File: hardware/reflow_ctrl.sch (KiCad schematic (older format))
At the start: 18 parts, among them IC1 MAX6675, U2 MOC3063, U3 BTA41/600B, X2 Mains, X3 Load, X4 Thermocouple

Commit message: ERC clean
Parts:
- gave numbers to parts that had none: 3
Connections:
- wire segments 49 -> 52
- no-connect marks 1 -> 5
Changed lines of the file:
@@
 L_load
 $Comp
-L GND #PWR01
+L GND #PWR7
 U 1 1 56A9FAD0
 P 6250 2150
-F 0 "#PWR01" H 6250 1900 50  0001 C CNN
+F 0 "#PWR7" H 6250 1900 50  0001 C CNN
 F 1 "GND" H 6250 2000 50  0000 C CNN
 F 2 "" H 6250 2150 60  0000 C CNN
@@
 $EndComp
 $Comp
-L GND #PWR02
+L GND #PWR9
 U 1 1 56AA0C93
 P 8200 5000
-F 0 "#PWR02" H 8200 4750 50  0001 C CNN
+F 0 "#PWR9" H 8200 4750 50  0001 C CNN
 F 1 "GND" H 8200 4850 50  0000 C CNN
 F 2 "" H 8200 5000 60  0000 C CNN
@@
 TODO\n* Complete supplier links\n* Add 3 Switches and approx. 3 LEDs\n* Add netclasses
 $Comp
-L CONN_02X05 X?
+L CONN_02X05 X1
 U 1 1 56C0B2E0
 P 3150 3400
-F 0 "X?" H 3150 3700 50  0000 C CNN
+F 0 "X1" H 3150 3700 50  0000 C CNN
 F 1 "Master" H 3150 3100 50  0000 C CNN
 F 2 "" H 3150 2200 60  0000 C CNN
@@
 $EndComp
 $Comp
-L +3.3V #PWR?
+L +3.3V #PWR8
 U 1 1 56C0C614
 P 8200 4600
-F 0 "#PWR?" H 8200 4450 50  0001 C CNN
+F 0 "#PWR8" H 8200 4450 50  0001 C CNN
 F 1 "+3.3V" H 8200 4740 50  0000 C CNN
 F 2 "" H 8200 4600 60  0000 C CNN
@@
 $EndComp
 $Comp
-L +3.3V #PWR?
+L +3.3V #PWR3
 U 1 1 56C0C64E
-P 2850 3150
-F 0 "#PWR?" H 2850 3000 50  0001 C CNN
-F 1 "+3.3V" H 2850 3290 50  0000 C CNN
-F 2 "" H 2850 3150 60  0000 C CNN
-F 3 "" H 2850 3150 60  0000 C CNN
-	1    2850 3150
-	1    0    0    -1
-$EndComp
-Wire Wire Line
-	2850 3150 2850 3200
+P 2850 2950
+F 0 "#PWR3" H 2850 2800 50  0001 C CNN
+F 1 "+3.3V" H 2850 3090 50  0000 C CNN
+F 2 "" H 2850 2950 60  0000 C CNN
+F 3 "" H 2850 2950 60  0000 C CNN
+	1    2850 2950
+	1    0    0    -1
+$EndComp
+Wire Wire Line
+	2850 2950 2850 3200
 Wire Wire Line
 	2850 3200 2900 3200
 $Comp
-L GND #PWR?
+L GND #PWR4
 U 1 1 56C0CE3A
 P 3450 3650
-F 0 "#PWR?" H 3450 3400 50  0001 C CNN
+F 0 "#PWR4" H 3450 3400 50  0001 C CNN
 F 1 "GND" H 3450 3500 50  0000 C CNN
 F 2 "" H 3450 3650 60  0000 C CNN
@@
 	3450 3600 3450 3650
 $Comp
-L C C?
+L C C1
 U 1 1 56C0D9F5
 P 1800 3350
-F 0 "C?" H 1800 3450 50  0000 L CNN
+F 0 "C1" H 1800 3450 50  0000 L CNN
 F 1 "100n" H 1800 3250 50  0000 L CNN
 F 2 "Capacitors_SMD:C_0603" H 1838 3200 30  0001 C CNN
@@
 $EndComp
 $Comp
-L C C?
+L C C2
 U 1 1 56C209CA
 P 2100 3350
-F 0 "C?" H 2100 3450 50  0000 L CNN
+F 0 "C2" H 2100 3450 50  0000 L CNN
 F 1 "100n" H 2100 3250 50  0000 L CNN
 F 2 "Capacitors_SMD:C_0603" H 2138 3200 30  0001 C CNN
@@
 $EndComp
 $Comp
-L GND #PWR?
+L GND #PWR2
 U 1 1 56C20A24
 P 1950 3600
-F 0 "#PWR?" H 1950 3350 50  0001 C CNN
+F 0 "#PWR2" H 1950 3350 50  0001 C CNN
 F 1 "GND" H 1950 3450 50  0000 C CNN
 F 2 "" H 1950 3600 60  0000 C CNN
@@
 Connection ~ 1950 3550
 $Comp
-L +3.3V #PWR?
+L +3.3V #PWR1
 U 1 1 56C20AF7
 P 1950 3100
-F 0 "#PWR?" H 1950 2950 50  0001 C CNN
+F 0 "#PWR1" H 1950 2950 50  0001 C CNN
 F 1 "+3.3V" H 1950 3240 50  0000 C CNN
 F 2 "" H 1950 3100 60  0000 C CNN
@@
 	1950 3100 1950 3150
 Connection ~ 1950 3150
+NoConn ~ 3400 3200
+NoConn ~ 3400 3300
+NoConn ~ 2900 3300
+NoConn ~ 3400 3400
+$Comp
+L PWR_FLAG #FLG1
+U 1 1 56C22014
+P 5900 7000
+F 0 "#FLG1" H 5900 7095 50  0001 C CNN
+F 1 "PWR_FLAG" V 5900 7350 50  0000 C CNN
+F 2 "" H 5900 7000 60  0000 C CNN
+F 3 "" H 5900 7000 60  0000 C CNN
+	1    5900 7000
+	0    1    1    0
+$EndComp
+$Comp
+L PWR_FLAG #FLG2
+U 1 1 56C22108
+P 5900 7200
+F 0 "#FLG2" H 5900 7295 50  0001 C CNN
+F 1 "PWR_FLAG" V 5900 7550 50  0000 C CNN
+F 2 "" H 5900 7200 60  0000 C CNN
+F 3 "" H 5900 7200 60  0000 C CNN
+	1    5900 7200
+	0    1    1    0
+$EndComp
+$Comp
+L GND #PWR6
+U 1 1 56C22149
+P 5850 7250
+F 0 "#PWR6" H 5850 7000 50  0001 C CNN
+F 1 "GND" H 5850 7100 50  0000 C CNN
+F 2 "" H 5850 7250 60  0000 C CNN
+F 3 "" H 5850 7250 60  0000 C CNN
+	1    5850 7250
+	1    0    0    -1
+$EndComp
+Wire Wire Line
+	5850 7250 5850 7200
+Wire Wire Line
+	5850 7200 5900 7200
+$Comp
+L +3.3V #PWR5
+U 1 1 56C22402
+P 5850 7000
+F 0 "#PWR5" H 5850 6850 50  0001 C CNN
+F 1 "+3.3V" H 5850 7140 50  0000 C CNN
+F 2 "" H 5850 7000 60  0000 C CNN
+F 3 "" H 5850 7000 60  0000 C CNN
+	1    5850 7000
+	0    -1   -1   0
+$EndComp
+Wire Wire Line
+	5850 7000 5900 7000
 $EndSCHEMATC

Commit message: Update board
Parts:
- X1: footprint (none) -> uMIDI:Con-boxed_header-THT
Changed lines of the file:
@@
 F 0 "X1" H 3150 3700 50  0000 C CNN
 F 1 "Master" H 3150 3100 50  0000 C CNN
-F 2 "" H 3150 2200 60  0000 C CNN
+F 2 "uMIDI:Con-boxed_header-THT" H 3150 2200 60  0001 C CNN
 F 3 "" H 3150 2200 60  0000 C CNN
 	1    3150 3400

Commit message: Prepare net classes
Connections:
- net labels added: L_main_fused, MOC_A1, MOC_A2, Snub
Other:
- moved on the sheet: C12, R6
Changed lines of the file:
@@
 L R R6
 U 1 1 56A9031F
-P 8550 1700
-F 0 "R6" V 8630 1700 50  0000 C CNN
-F 1 "39" V 8550 1700 50  0000 C CNN
-F 2 "Resistors_SMD:R_1206" V 8480 1700 30  0001 C CNN
-F 3 "" H 8550 1700 30  0000 C CNN
-	1    8550 1700
+P 8550 1650
+F 0 "R6" V 8630 1650 50  0000 C CNN
+F 1 "39" V 8550 1650 50  0000 C CNN
+F 2 "Resistors_SMD:R_1206" V 8480 1650 30  0001 C CNN
+F 3 "" H 8550 1650 30  0000 C CNN
+	1    8550 1650
 	1    0    0    -1
 $EndComp
@@
 L C C12
 U 1 1 56A90389
-P 8550 2200
-F 0 "C12" H 8650 2350 50  0000 L CNN
-F 1 "10n" H 8650 2250 50  0000 L CNN
-F 2 "Capacitors_SMD:C_1206" H 8588 2050 30  0001 C CNN
-F 3 "" H 8550 2200 60  0000 C CNN
-F 4 "630V" H 8650 2050 60  0000 L CNN "Voltage"
-F 5 "X7R" H 8650 2150 60  0000 L CNN "Dielectric"
-	1    8550 2200
+P 8550 2300
+F 0 "C12" H 8650 2450 50  0000 L CNN
+F 1 "10n" H 8650 2350 50  0000 L CNN
+F 2 "Capacitors_SMD:C_1206" H 8588 2150 30  0001 C CNN
+F 3 "" H 8550 2300 60  0000 C CNN
+F 4 "630V" H 8650 2150 60  0000 L CNN "Voltage"
+F 5 "X7R" H 8650 2250 60  0000 L CNN "Dielectric"
+	1    8550 2300
 	1    0    0    -1
 $EndComp
@@
 L_load
 $Comp
-L GND #PWR7
+L GND #PWR01
 U 1 1 56A9FAD0
 P 6250 2150
-F 0 "#PWR7" H 6250 1900 50  0001 C CNN
+F 0 "#PWR01" H 6250 1900 50  0001 C CNN
 F 1 "GND" H 6250 2000 50  0000 C CNN
 F 2 "" H 6250 2150 60  0000 C CNN
@@
 $EndComp
 $Comp
-L GND #PWR9
+L GND #PWR02
 U 1 1 56AA0C93
 P 8200 5000
-F 0 "#PWR9" H 8200 4750 50  0001 C CNN
+F 0 "#PWR02" H 8200 4750 50  0001 C CNN
 F 1 "GND" H 8200 4850 50  0000 C CNN
 F 2 "" H 8200 5000 60  0000 C CNN
@@
 	7000 2650 10200 2650
 Wire Wire Line
-	8550 2350 8550 2650
-Wire Wire Line
-	8550 2050 8550 1850
+	8550 2450 8550 2650
+Wire Wire Line
+	8550 2150 8550 1800
 Wire Wire Line
 	7000 1450 7000 1350
@@
 	7000 1350 9350 1350
 Wire Wire Line
-	8550 1550 8550 1350
+	8550 1500 8550 1350
 Connection ~ 8550 1350
 Connection ~ 7000 2100
@@
 $EndComp
 $Comp
-L +3.3V #PWR8
+L +3.3V #PWR03
 U 1 1 56C0C614
 P 8200 4600
-F 0 "#PWR8" H 8200 4450 50  0001 C CNN
+F 0 "#PWR03" H 8200 4450 50  0001 C CNN
 F 1 "+3.3V" H 8200 4740 50  0000 C CNN
 F 2 "" H 8200 4600 60  0000 C CNN
@@
 $EndComp
 $Comp
-L +3.3V #PWR3
+L +3.3V #PWR04
 U 1 1 56C0C64E
 P 2850 2950
-F 0 "#PWR3" H 2850 2800 50  0001 C CNN
+F 0 "#PWR04" H 2850 2800 50  0001 C CNN
 F 1 "+3.3V" H 2850 3090 50  0000 C CNN
 F 2 "" H 2850 2950 60  0000 C CNN
@@
 	2850 3200 2900 3200
 $Comp
-L GND #PWR4
+L GND #PWR05
 U 1 1 56C0CE3A
 P 3450 3650
-F 0 "#PWR4" H 3450 3400 50  0001 C CNN
+F 0 "#PWR05" H 3450 3400 50  0001 C CNN
 F 1 "GND" H 3450 3500 50  0000 C CNN
 F 2 "" H 3450 3650 60  0000 C CNN
@@
 $EndComp
 $Comp
-L GND #PWR2
+L GND #PWR06
 U 1 1 56C20A24
 P 1950 3600
-F 0 "#PWR2" H 1950 3350 50  0001 C CNN
+F 0 "#PWR06" H 1950 3350 50  0001 C CNN
 F 1 "GND" H 1950 3450 50  0000 C CNN
 F 2 "" H 1950 3600 60  0000 C CNN
@@
 Connection ~ 1950 3550
 $Comp
-L +3.3V #PWR1
+L +3.3V #PWR07
 U 1 1 56C20AF7
 P 1950 3100
-F 0 "#PWR1" H 1950 2950 50  0001 C CNN
+F 0 "#PWR07" H 1950 2950 50  0001 C CNN
 F 1 "+3.3V" H 1950 3240 50  0000 C CNN
 F 2 "" H 1950 3100 60  0000 C CNN
@@
 NoConn ~ 3400 3400
 $Comp
-L PWR_FLAG #FLG1
+L PWR_FLAG #FLG08
 U 1 1 56C22014
 P 5900 7000
-F 0 "#FLG1" H 5900 7095 50  0001 C CNN
+F 0 "#FLG08" H 5900 7095 50  0001 C CNN
 F 1 "PWR_FLAG" V 5900 7350 50  0000 C CNN
 F 2 "" H 5900 7000 60  0000 C CNN
@@
 $EndComp
 $Comp
-L PWR_FLAG #FLG2
+L PWR_FLAG #FLG09
 U 1 1 56C22108
 P 5900 7200
-F 0 "#FLG2" H 5900 7295 50  0001 C CNN
+F 0 "#FLG09" H 5900 7295 50  0001 C CNN
 F 1 "PWR_FLAG" V 5900 7550 50  0000 C CNN
 F 2 "" H 5900 7200 60  0000 C CNN
@@
 $EndComp
 $Comp
-L GND #PWR6
+L GND #PWR010
 U 1 1 56C22149
 P 5850 7250
-F 0 "#PWR6" H 5850 7000 50  0001 C CNN
+F 0 "#PWR010" H 5850 7000 50  0001 C CNN
 F 1 "GND" H 5850 7100 50  0000 C CNN
 F 2 "" H 5850 7250 60  0000 C CNN
@@
 	5850 7200 5900 7200
 $Comp
-L +3.3V #PWR5
+L +3.3V #PWR011
 U 1 1 56C22402
 P 5850 7000
-F 0 "#PWR5" H 5850 6850 50  0001 C CNN
+F 0 "#PWR011" H 5850 6850 50  0001 C CNN
 F 1 "+3.3V" H 5850 7140 50  0000 C CNN
 F 2 "" H 5850 7000 60  0000 C CNN
@@
 Wire Wire Line
 	5850 7000 5900 7000
+Text Label 6950 1900 0    60   ~ 0
+MOC_A1
+Text Label 6950 2100 0    60   ~ 0
+MOC_A2
+Text Label 8550 2100 1    60   ~ 0
+Snub
+Text Label 8350 1350 0    60   ~ 0
+L_main_fused
 $EndSCHEMATC

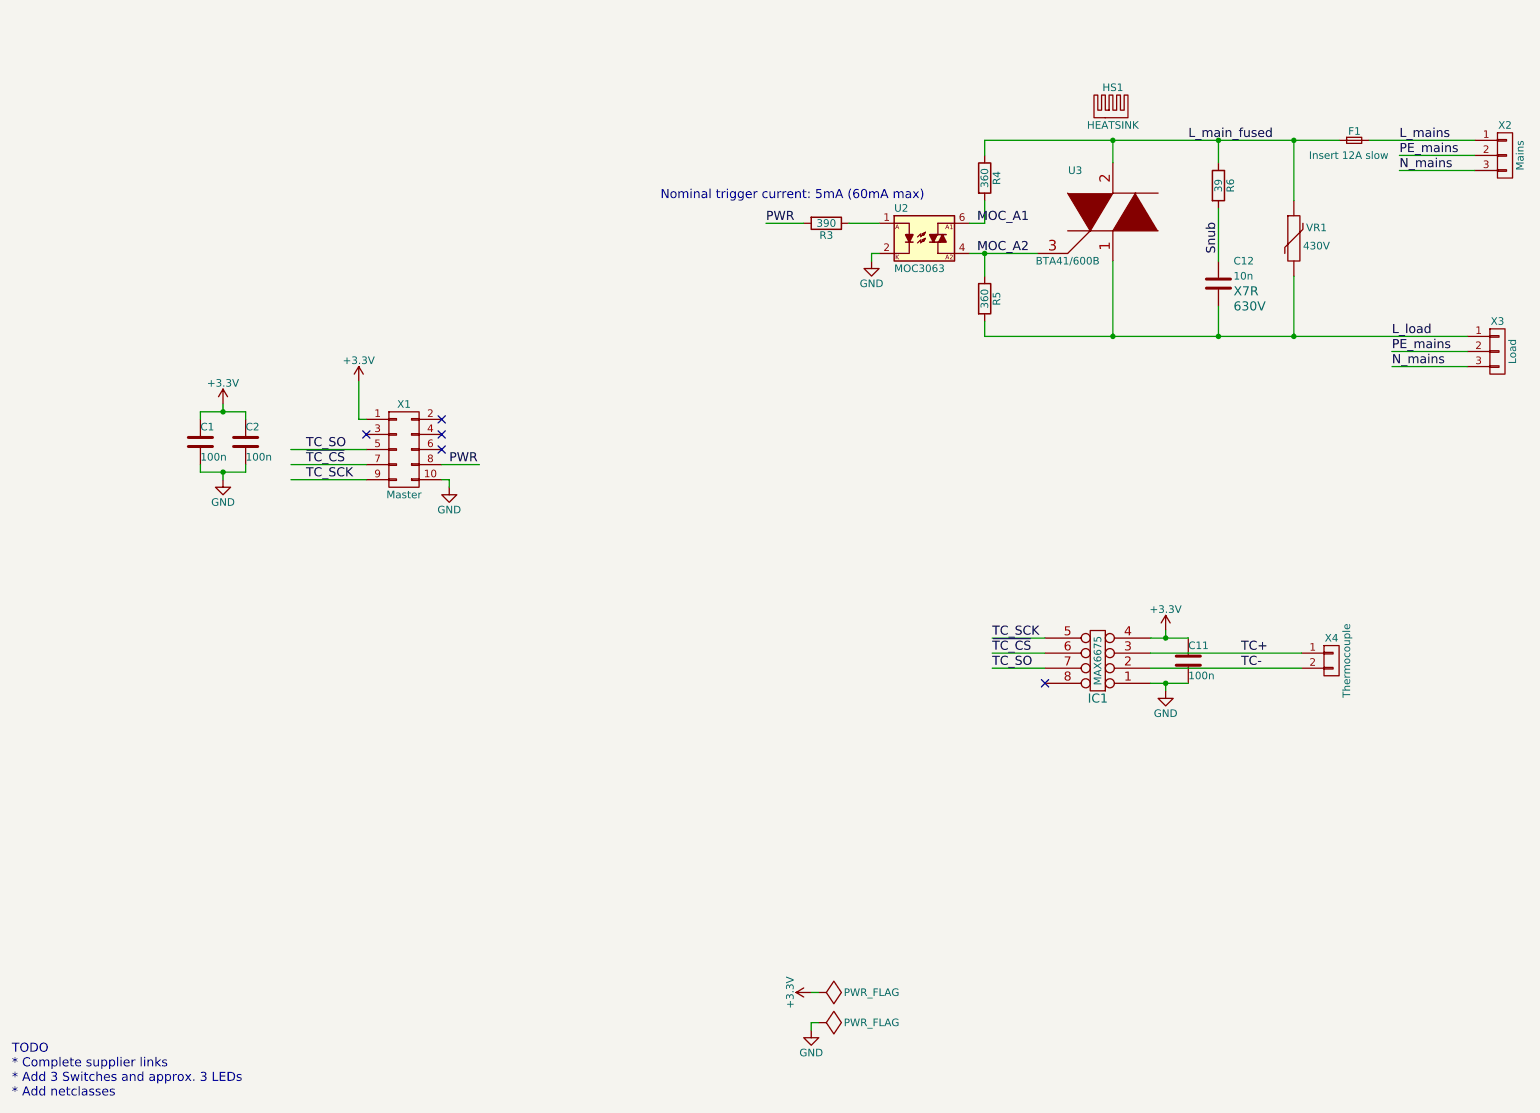
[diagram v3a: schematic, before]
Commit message: Shrink schematic page size
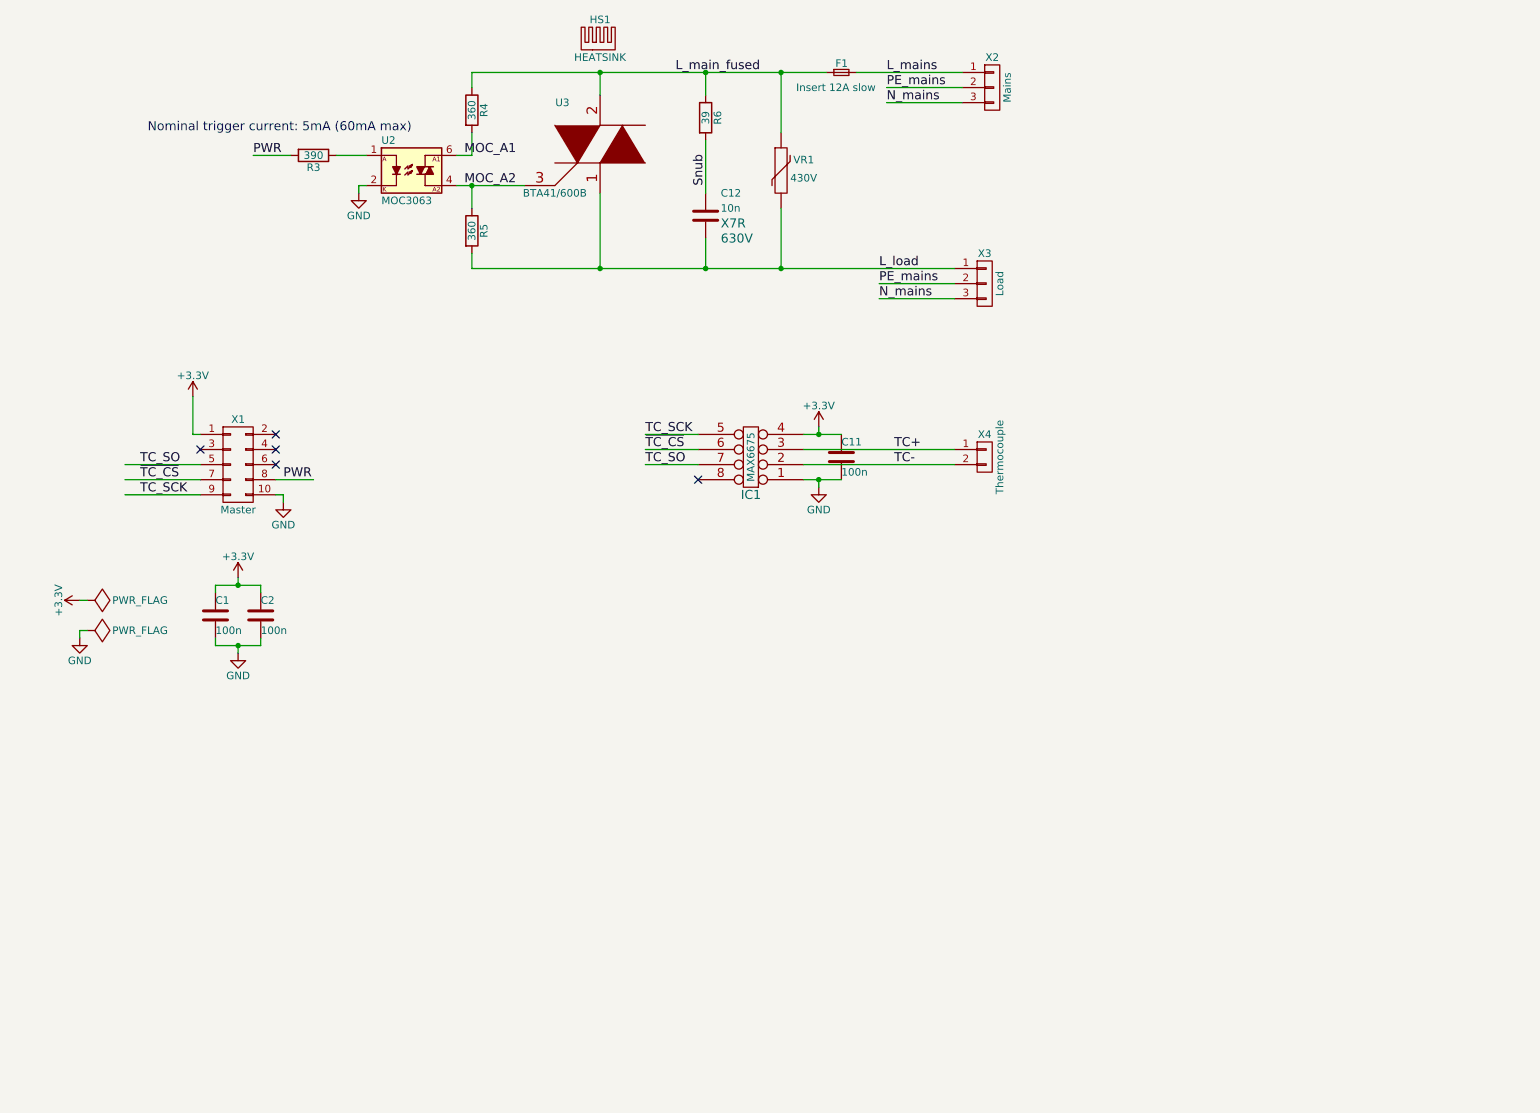
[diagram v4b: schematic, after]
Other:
- note removed: "TODO\n* Complete supplier links\n* Add 3 Switches and approx. 3 LEDs\n* Add netclasses"
- moved on the sheet: C1, C11, C12, C2, F1, HS1, IC1, R3, R4, R5, R6, U2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

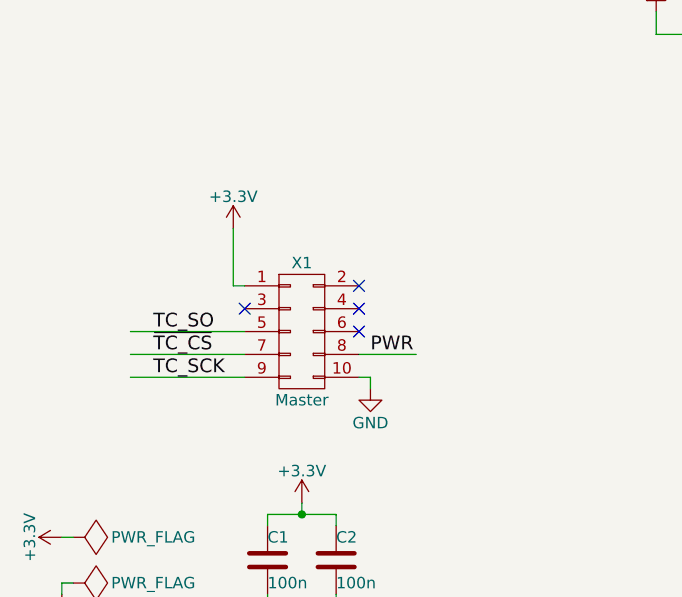
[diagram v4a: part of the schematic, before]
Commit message: Disentangle connector pinout; Start placement
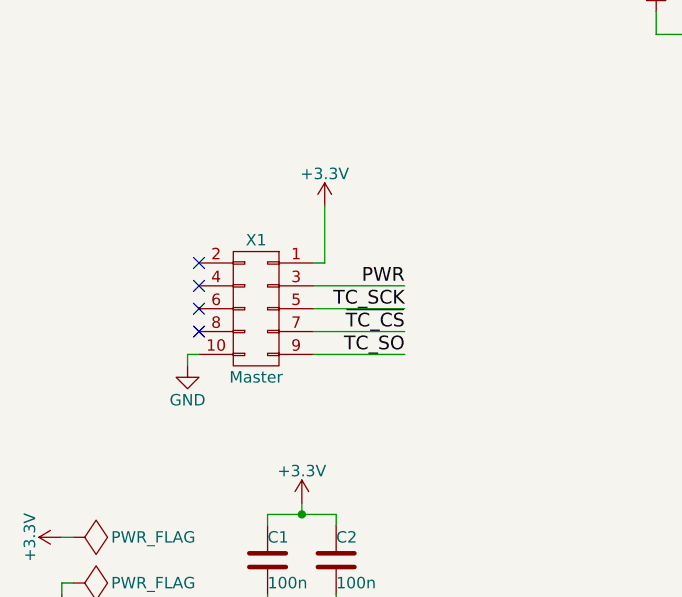
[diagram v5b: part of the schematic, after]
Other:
- moved on the sheet: X1
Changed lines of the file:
@@
 	1    0    0    -1
 $EndComp
-Text Label 1400 3700 0    60   ~ 0
+Text Label 2500 3400 2    60   ~ 0
 TC_SCK
-Text Label 1400 3600 0    60   ~ 0
+Text Label 2500 3500 2    60   ~ 0
 ~TC_CS
-Text Label 1400 3500 0    60   ~ 0
+Text Label 2500 3600 2    60   ~ 0
 TC_SO
-Text Label 2350 3600 0    60   ~ 0
+Text Label 2500 3300 2    60   ~ 0
 PWR
 $Comp
@@
 	6300 2400 6800 2400
 Wire Wire Line
-	1300 3500 1800 3500
-Wire Wire Line
-	1300 3600 1800 3600
-Wire Wire Line
-	1300 3700 1800 3700
-Wire Wire Line
 	5650 1800 5650 2200
 Connection ~ 5650 2200
@@
 	5650 900  5650 1300
 Connection ~ 5650 900
-Wire Wire Line
-	2300 3600 2550 3600
 Text Notes 1450 1300 0    60   ~ 0
 Nominal trigger current: 5mA (60mA max)
@@
 L CONN_02X05 X1
 U 1 1 56C0B2E0
-P 2050 3500
-F 0 "X1" H 2050 3800 50  0000 C CNN
-F 1 "Master" H 2050 3200 50  0000 C CNN
-F 2 "uMIDI:Con-boxed_header-THT" H 2050 2300 60  0001 C CNN
-F 3 "" H 2050 2300 60  0000 C CNN
-	1    2050 3500
-	1    0    0    -1
+P 1850 3400
+F 0 "X1" H 1850 3700 50  0000 C CNN
+F 1 "Master" H 1850 3100 50  0000 C CNN
+F 2 "uMIDI:Con-boxed_header-THT" H 1850 2200 60  0001 C CNN
+F 3 "" H 1850 2200 60  0000 C CNN
+	1    1850 3400
+	-1   0    0    -1
 $EndComp
 $Comp
@@
 L +3.3V #PWR04
 U 1 1 56C0C64E
-P 1750 3050
-F 0 "#PWR04" H 1750 2900 50  0001 C CNN
-F 1 "+3.3V" H 1750 3190 50  0000 C CNN
-F 2 "" H 1750 3050 60  0000 C CNN
-F 3 "" H 1750 3050 60  0000 C CNN
-	1    1750 3050
-	1    0    0    -1
-$EndComp
-Wire Wire Line
-	1750 3050 1750 3300
-Wire Wire Line
-	1750 3300 1800 3300
+P 2150 2950
+F 0 "#PWR04" H 2150 2800 50  0001 C CNN
+F 1 "+3.3V" H 2150 3090 50  0000 C CNN
+F 2 "" H 2150 2950 60  0000 C CNN
+F 3 "" H 2150 2950 60  0000 C CNN
+	1    2150 2950
+	-1   0    0    -1
+$EndComp
+Wire Wire Line
+	2150 2950 2150 3200
+Wire Wire Line
+	2150 3200 2100 3200
 $Comp
 L GND #PWR05
 U 1 1 56C0CE3A
-P 2350 3750
-F 0 "#PWR05" H 2350 3500 50  0001 C CNN
-F 1 "GND" H 2350 3600 50  0000 C CNN
-F 2 "" H 2350 3750 60  0000 C CNN
-F 3 "" H 2350 3750 60  0000 C CNN
-	1    2350 3750
-	1    0    0    -1
-$EndComp
-Wire Wire Line
-	2300 3700 2350 3700
-Wire Wire Line
-	2350 3700 2350 3750
+P 1550 3650
+F 0 "#PWR05" H 1550 3400 50  0001 C CNN
+F 1 "GND" H 1550 3500 50  0000 C CNN
+F 2 "" H 1550 3650 60  0000 C CNN
+F 3 "" H 1550 3650 60  0000 C CNN
+	1    1550 3650
+	-1   0    0    -1
+$EndComp
+Wire Wire Line
+	1600 3600 1550 3600
+Wire Wire Line
+	1550 3600 1550 3650
 $Comp
 L C C1
@@
 	2050 4250 2050 4300
 Connection ~ 2050 4300
-NoConn ~ 2300 3300
-NoConn ~ 2300 3400
-NoConn ~ 1800 3400
-NoConn ~ 2300 3500
+NoConn ~ 1600 3200
+NoConn ~ 1600 3300
+NoConn ~ 1600 3400
 $Comp
 L PWR_FLAG #FLG08
@@
 Text Label 4950 900  0    60   ~ 0
 L_main_fused
+Wire Wire Line
+	2500 3400 2100 3400
+Wire Wire Line
+	2500 3600 2100 3600
+Wire Wire Line
+	2500 3500 2100 3500
+Wire Wire Line
+	2500 3300 2100 3300
+NoConn ~ 1600 3500
 $EndSCHEMATC
